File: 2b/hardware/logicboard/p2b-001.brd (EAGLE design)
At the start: 91 x 90 mm, 72 parts, among them IC1 74LS06N, IC2 4066N, J1 MKR, J10 1-Wire, J2 GPIO, J20 GPIO, J3 Vcc, J4** RLY2, J5 SPI, J6 LED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

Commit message: Fixed P2b.
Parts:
- added RZ01, RZ02, RZ03, RZ04: Inf, rcl:M2012
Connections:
- net ANLG0: now also RZ01.2
- net ANLG0R: now also RZ01.1
- net ANLG1: now also RZ02.2
- net ANLG1R: now also RZ02.1
- net ANLG2: now also RZ03.2
- net ANLG2R: now also RZ03.1
- net ANLG3: now also RZ04.2
- net ANLG3R: now also RZ04.1
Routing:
- net RLYOUT2: track 83.3 -> 179.1 mm, vias 3 -> 0
- net SDA: track 178.4 -> 271.8 mm, vias 6 -> 9
- net GND: track 453.6 -> 519.0 mm, vias 7 -> 6
- net ANLG1: track 124.6 -> 64.0 mm, vias 4 -> 5
- net V+: track 230.9 -> 174.6 mm, vias 4 -> 7
- net MNTR: track 115.9 -> 60.7 mm, vias 0 -> 3
- net ANLG2: track 155.2 -> 112.5 mm, vias 5 -> 8
- net DTCT1: track 84.2 -> 126.9 mm, vias 3 -> 4
- net TX: track 61.1 -> 102.6 mm, vias 3 -> 0
- net SCL: track 271.2 -> 230.2 mm, vias 6 -> 5
- net ANLG0: track 80.5 -> 47.4 mm, vias 3 -> 1
- net DTCT2: track 84.3 -> 112.5 mm, vias 3 -> 2
- net GPIO1: track 179.9 -> 153.3 mm, vias 2 -> 5
- net VCC/2: track 169.8 -> 145.8 mm, vias 7 -> 6
- net RLYOUT: track 102.1 -> 82.8 mm, vias 0 -> 7
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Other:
- board text added: "Bridge to bypass 4066"
- board text removed: "Bridge 4 segments to bypass"

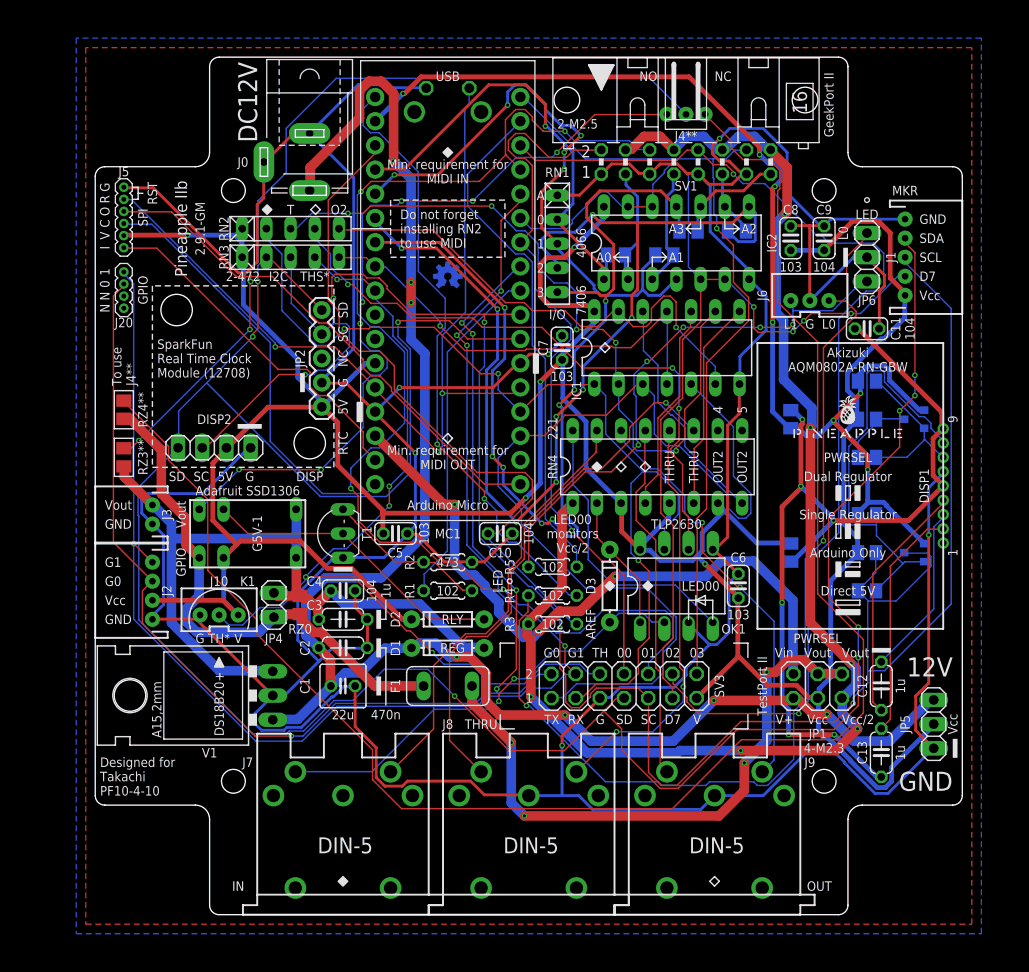
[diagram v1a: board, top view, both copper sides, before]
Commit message: Fixed caps.
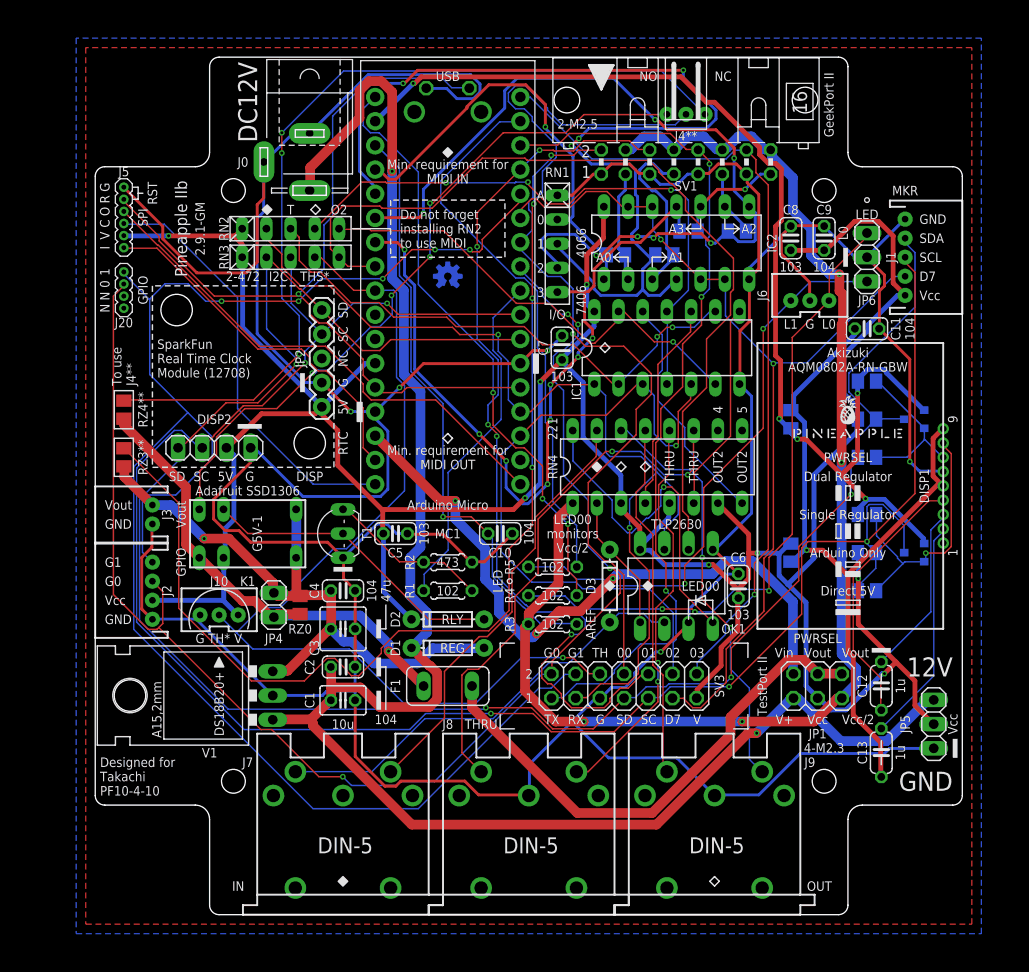
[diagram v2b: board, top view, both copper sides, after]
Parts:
- C1: value 22u -> 10u; device rcl:C025-050X050 -> rcl:C025-030X050
- C2: value 470n -> 100n; device rcl:C050-024X044 -> rcl:C025-024X044
- C3: value 1u -> 47u; device rcl:C050-024X044 -> rcl:C025-050X050
- moved C2 2.00 mm to (26.0, 26.0)
- moved C1 1.50 mm to (26.0, 22.5)
- moved C3 1.00 mm to (26.0, 30.0)
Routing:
- net RLYOUT2: track 179.1 -> 93.4 mm, vias 0 -> 3
- net SDA: track 271.8 -> 208.7 mm, vias 9 -> 4
- net RLYOUT1: track 86.8 -> 142.2 mm
- net ANLG1: track 64.0 -> 108.6 mm, vias 5 -> 4
- net GND: track 519.0 -> 479.5 mm, vias 6 -> 5
- net LED0A: track 106.4 -> 68.8 mm, vias 2 -> 3
- net DTCT2: track 112.5 -> 79.1 mm, vias 2 -> 3
- net MNTR: track 60.7 -> 92.1 mm, vias 3 -> 0
- net DTCT1: track 126.9 -> 95.6 mm, vias 4 -> 5
- net ANLG3: track 104.3 -> 81.2 mm
- net ANLG2: track 112.5 -> 89.6 mm, vias 8 -> 7
- net NMTRTN: track 77.5 -> 56.5 mm, vias 5 -> 2
- net TX: track 102.6 -> 82.7 mm, vias 0 -> 1
- net VCC: track 351.1 -> 332.5 mm, vias 5 -> 8
- net GPIO1: track 153.3 -> 170.9 mm
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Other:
- board text added: "10u"
- board text added: "47u"
- board text removed: "22u"
- board text removed: "470n"

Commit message: Now P2b has phantom power.
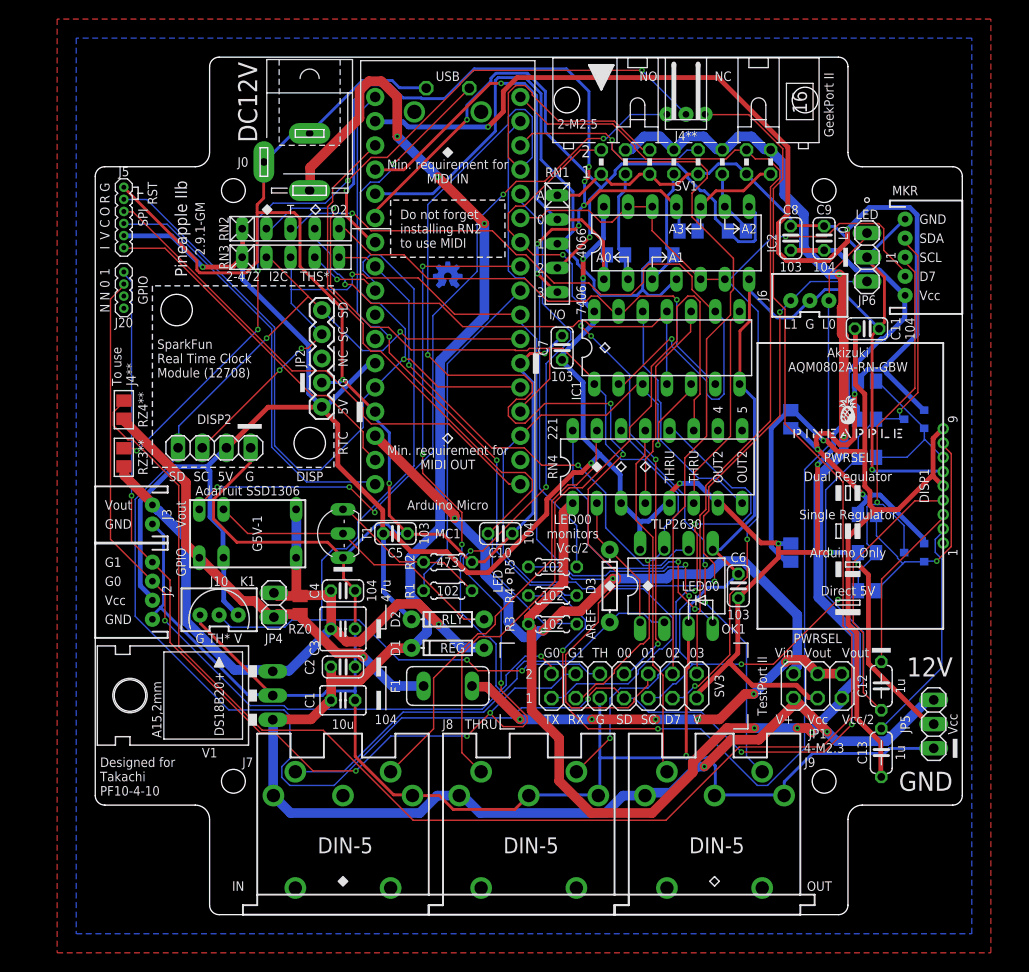
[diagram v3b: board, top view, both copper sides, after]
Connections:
- net GND: now also J7.1, J8.1, J9.1
- net V+: now also J7.3, J8.3, J9.3
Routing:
- net RLYOUT2: track 93.4 -> 185.3 mm, vias 3 -> 0
- net RLYOUT1: track 142.2 -> 84.4 mm, vias 3 -> 5
- net DTCT1: track 95.6 -> 141.9 mm, vias 5 -> 3
- net ANLG1: track 108.6 -> 65.1 mm, vias 4 -> 0
- net SCL: track 221.1 -> 180.2 mm, vias 5 -> 8
- net LED0A: track 68.8 -> 104.1 mm, vias 3 -> 2
- net MNTR: track 92.1 -> 56.9 mm, vias 0 -> 2
- net NMTRTN: track 56.5 -> 79.9 mm
- net MTRTN: track 55.9 -> 78.0 mm, vias 2 -> 0
- net VDD: track 118.8 -> 140.8 mm
- net SDA: track 208.7 -> 228.7 mm, vias 4 -> 6
- net RST: track 89.0 -> 104.7 mm, vias 1 -> 2
- net VCC/VDD: track 77.9 -> 92.6 mm
- net VCC/2: track 138.6 -> 153.2 mm, vias 4 -> 5
- net ANLG2: track 89.6 -> 75.3 mm, vias 7 -> 2
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
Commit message: Added SW.
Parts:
- added S2: (no value), switch-dil:DIP02YL
- V1: device v-reg:78XXL -> v-reg:78XXS
- moved V1 3.50 mm to (11.3, 23.0)
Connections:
- new net MIDIINV+: J7.3, S2.1
- new net MIDIOUTV+: J8.3, J9.3, S2.2
- net V+: now also S2.3, S2.4; no longer J7.3, J8.3, J9.3
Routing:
- net VOUT: track 43.5 -> 167.7 mm, vias 6 -> 10
- net RLYOUT2: track 185.3 -> 80.7 mm, vias 0 -> 5
- net MIDIOUTV+: track 0.00 -> 56.2 mm
- net DTCT1: track 141.9 -> 92.4 mm, vias 3 -> 4
- net MNTR: track 56.9 -> 100.3 mm, vias 2 -> 1
- net SCL: track 180.2 -> 223.1 mm, vias 8 -> 5
- net RLYOUT: track 80.4 -> 110.8 mm, vias 5 -> 0
- net LED0A: track 104.1 -> 76.5 mm
- net NMTRTN: track 79.9 -> 56.0 mm, vias 2 -> 1
- net VCC: track 321.4 -> 344.7 mm, vias 9 -> 6
- net RLYOUT1: track 84.4 -> 107.3 mm, vias 5 -> 1
- net VDD: track 140.8 -> 121.3 mm, vias 5 -> 7
- net ANLG1: track 65.1 -> 84.3 mm, vias 0 -> 4
- net RST: track 104.7 -> 85.6 mm, vias 2 -> 5
- net MIDIINV+: track 0.00 -> 17.5 mm
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- removed copper zone on layer 1, net GND
- removed copper zone on layer 16, net GND

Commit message: Now has a phantom SW.
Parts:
- S2: device switch-dil:DIP02YL -> switch-dil:DIP04YL
- moved V1 6.26 mm to (17.5, 24.0), turned to 0 degrees
- moved S2 0.71 mm to (6.50, 22.5), turned to 90 degrees
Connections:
- new net MIDIINGND: J7.1, S2.1
- new net MIDIOUTGND: J8.1, J9.1, S2.3
- net GND: now also S2.6, S2.8; no longer J7.1, J8.1, J9.1
- net MIDIINV+: now also S2.2; no longer S2.1
- net MIDIOUTV+: now also S2.4; no longer S2.2
- net V+: now also S2.5, S2.7; no longer S2.3, S2.4
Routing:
- net VOUT: track 167.7 -> 59.6 mm, vias 10 -> 5
- net MIDIOUTGND: track 0.00 -> 69.4 mm, vias 0 -> 1
- net SDA: track 224.7 -> 179.6 mm, vias 6 -> 8
- net LED0: track 65.9 -> 103.5 mm
- net VDD: track 121.3 -> 153.2 mm, vias 7 -> 14
- net MIDIINGND: track 0.00 -> 25.6 mm
- net VCC/2: track 140.7 -> 165.5 mm, vias 4 -> 7
- net TX: track 75.2 -> 51.3 mm, vias 1 -> 0
- net VCC/VDD: track 102.0 -> 78.9 mm, vias 6 -> 2
- net RLYOUT: track 110.8 -> 88.2 mm, vias 0 -> 1
- net GPIO1: track 159.3 -> 137.5 mm
- net DTCT0: track 81.7 -> 101.6 mm, vias 2 -> 3
- net RLYOUT1: track 107.3 -> 87.5 mm
- net DTCT1: track 92.4 -> 75.8 mm, vias 4 -> 3
- net MTRTN: track 68.3 -> 52.8 mm, vias 3 -> 2
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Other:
- board text added: "Phantom"

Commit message: GND pattern.
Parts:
- S2: value (none) -> MIDIPHANTOM
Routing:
- added copper zone on layer 1, net GND
- added copper zone on layer 16, net GND
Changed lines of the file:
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@@
 <setting verticaltext="up"/>
 </settings>
-<grid distance="0.5" unitdist="mm" unit="mm" style="lines" multiple="2" display="yes" altdistance="50" altunitdist="mil" altunit="mil"/>
+<grid distance="2" unitdist="mm" unit="mm" style="lines" multiple="2" display="yes" altdistance="50" altunitdist="mil" altunit="mil"/>
 <layers>
-<layer number="1" name="Top" color="4" fill="1" visible="no" active="yes"/>
-<layer number="16" name="Bottom" color="1" fill="1" visible="no" active="yes"/>
+<layer number="1" name="Top" color="4" fill="1" visible="yes" active="yes"/>
+<layer number="16" name="Bottom" color="1" fill="1" visible="yes" active="yes"/>
 <layer number="17" name="Pads" color="2" fill="1" visible="yes" active="yes"/>
 <layer number="18" name="Vias" color="2" fill="1" visible="yes" active="yes"/>
@@
 <attribute name="VALUE" x="63.54" y="69.21" size="1.27" layer="28" rot="MR0"/>
 </element>
-<element name="S2" library="switch-dil" library_urn="urn:adsk.eagle:library:375" package="DIP04YL" package3d_urn="urn:adsk.eagle:package:27255/2" value="" x="6.5" y="22.5" smashed="yes" rot="R90">
+<element name="S2" library="switch-dil" library_urn="urn:adsk.eagle:library:375" package="DIP04YL" package3d_urn="urn:adsk.eagle:package:27255/2" value="MIDIPHANTOM" x="6.5" y="22.5" smashed="yes" rot="R90">
 <attribute name="MF" value="" x="6.5" y="22.5" size="1.778" layer="27" rot="R90" display="off"/>
 <attribute name="MPN" value="" x="6.5" y="22.5" size="1.778" layer="27" rot="R90" display="off"/>
@@
 <via x="87.1728" y="39.8526" extent="1-16" drill="0.3048"/>
 <via x="47.0916" y="58.8264" extent="1-16" drill="0.3048"/>
+<polygon width="0.2" layer="1">
+<vertex x="-2" y="-2"/>
+<vertex x="94" y="-2"/>
+<vertex x="94" y="92"/>
+<vertex x="-2" y="92"/>
+</polygon>
+<polygon width="0.2" layer="16">
+<vertex x="-4" y="-4"/>
+<vertex x="96" y="-4"/>
+<vertex x="96" y="94"/>
+<vertex x="-4" y="94"/>
+</polygon>
 </signal>
 <signal name="VCC" class="2">

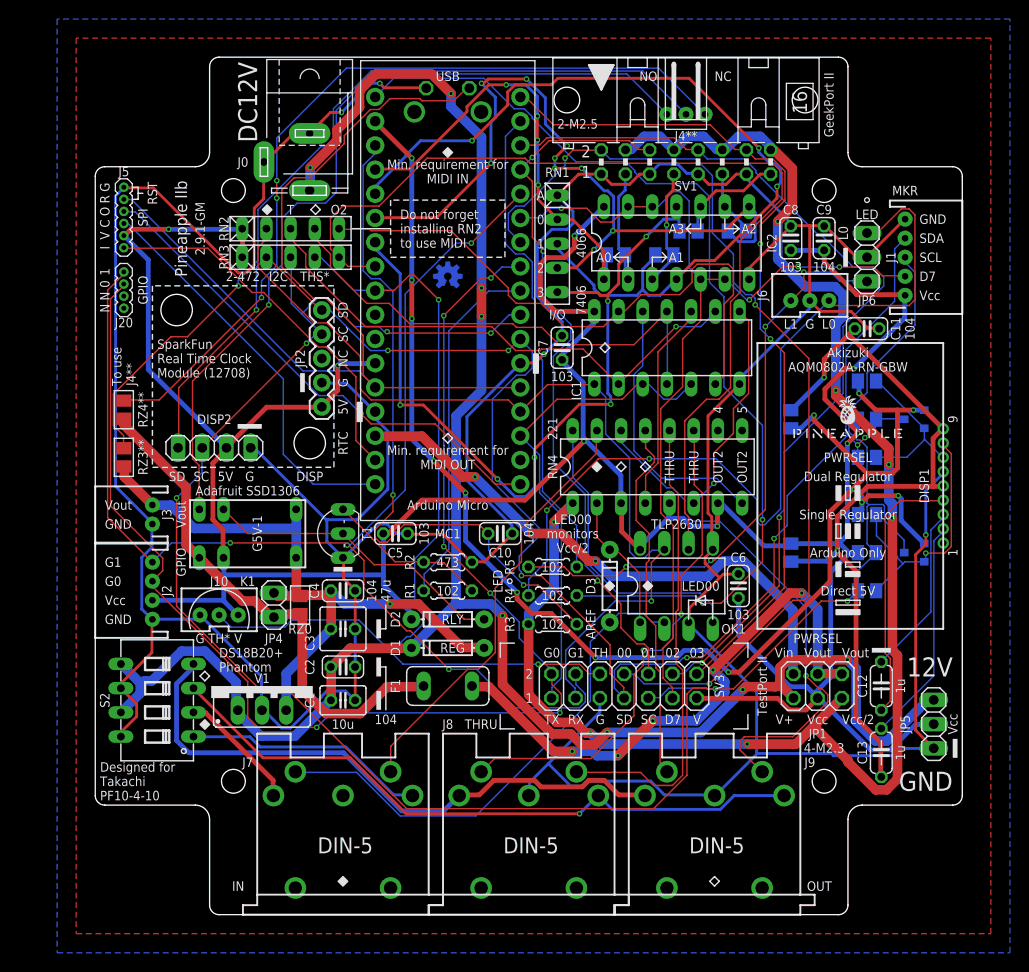
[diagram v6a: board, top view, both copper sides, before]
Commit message: vdd/vcc xbar for lcd monitor.
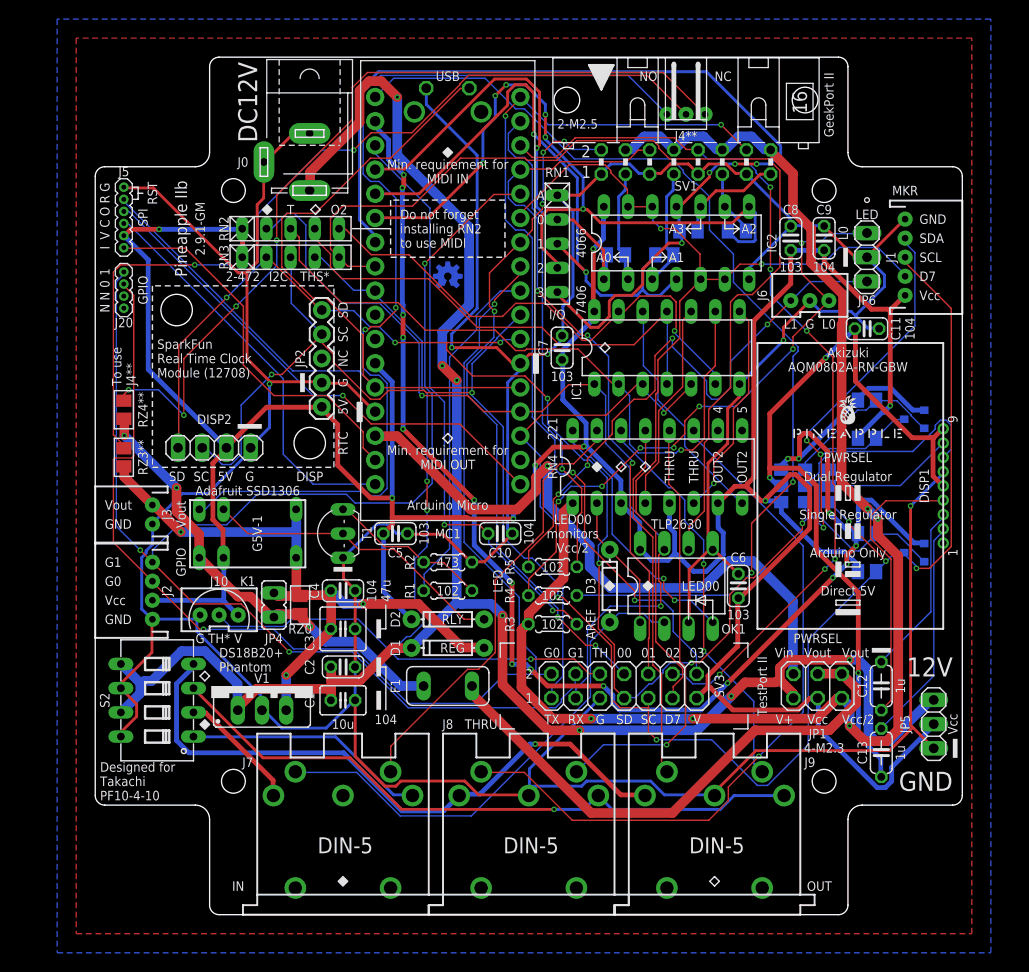
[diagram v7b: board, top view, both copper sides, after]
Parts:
- removed RZ1***, RZ2***, VCCBRIDGE***: Inf, rcl:M2012
- removed VDDBRIDGE: 0, rcl:M2012
- added JMP1, JMP2, JMP3: 0R-JUMPA, jump-0r-smd:A0R-JMP
- JP4: device pinhead:1X02 -> jumper:JP1
- moved R101 2.00 mm to (81.0, 36.0)
- moved R102 2.00 mm to (81.0, 40.0)
- moved R103 2.00 mm to (81.0, 50.0)
- moved R104 2.00 mm to (81.0, 54.0)
- turned JP4 to 180 degrees
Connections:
- removed net VCC/VDD: C11.1, C13.1, DISP1.5, DISP1.9, VCCBRIDGE***.1, VDDBRIDGE.1
- new net SCL3V/5V: DISP1.8, JMP3.2
- new net SDA3V/5V: DISP1.7, JMP2.2
- new net VDD/VCC: C11.1, C13.1, DISP1.5, DISP1.9, JMP1.2
- net SCL: now also JMP3.3; no longer RZ1***.1
- net SCL3V: now also JMP3.1; no longer DISP1.8, RZ1***.2
- net SDA: now also JMP2.3; no longer RZ2***.1
- net SDA3V: now also JMP2.1; no longer DISP1.7, RZ2***.2
- net VCC: now also JMP1.3; no longer VCCBRIDGE***.2
- net VDD: now also JMP1.1; no longer VDDBRIDGE.2
- net VOUTRAW: now also JP4.1; no longer JP4.2
- net VOUTRAW2: now also JP4.2; no longer JP4.1
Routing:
- net VDD/VCC: track 0.00 -> 83.0 mm, vias 0 -> 3
- net VCC/VDD: track 78.9 -> 0.00 mm, vias 2 -> 0
- net DTCT0: track 101.6 -> 72.8 mm, vias 3 -> 6
- net VCC: track 332.3 -> 359.1 mm
- net ANLG1: track 91.0 -> 64.3 mm, vias 3 -> 2
- net LED0A: track 90.1 -> 64.7 mm, vias 2 -> 7
- net MTRTN: track 52.8 -> 75.8 mm, vias 2 -> 1
- net SDA3V/5V: track 0.00 -> 22.9 mm
- net ANLG3: track 83.6 -> 103.5 mm, vias 6 -> 4
- net SCL: track 221.4 -> 202.6 mm, vias 6 -> 7
- net GPIO1: track 137.5 -> 156.2 mm, vias 4 -> 3
- net NMTRTN: track 56.1 -> 72.2 mm
- net RLYOUT: track 88.2 -> 102.5 mm, vias 1 -> 2
- net SCL3V/5V: track 0.00 -> 13.9 mm
- net VCC/2: track 165.5 -> 152.2 mm, vias 7 -> 5
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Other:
- board text added: "3.3V"
- board text removed: "3.3V I2C"
- board text removed: "5V I2C***"
